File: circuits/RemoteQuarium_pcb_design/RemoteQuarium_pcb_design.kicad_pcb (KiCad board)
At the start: 2 copper layers, 68.6 x 99.1 mm, 20 parts, among them J1 Power_terminal, J10 LCD_pins, J11 Ph_sensor_sockets, J12 ESP_pins, J13 TX_RX, J14 3.3V_GND, J2 ESP left side sockets, J3 ESP right side sockets, J4 Relay_terminal, J5 Relay_in4_socket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

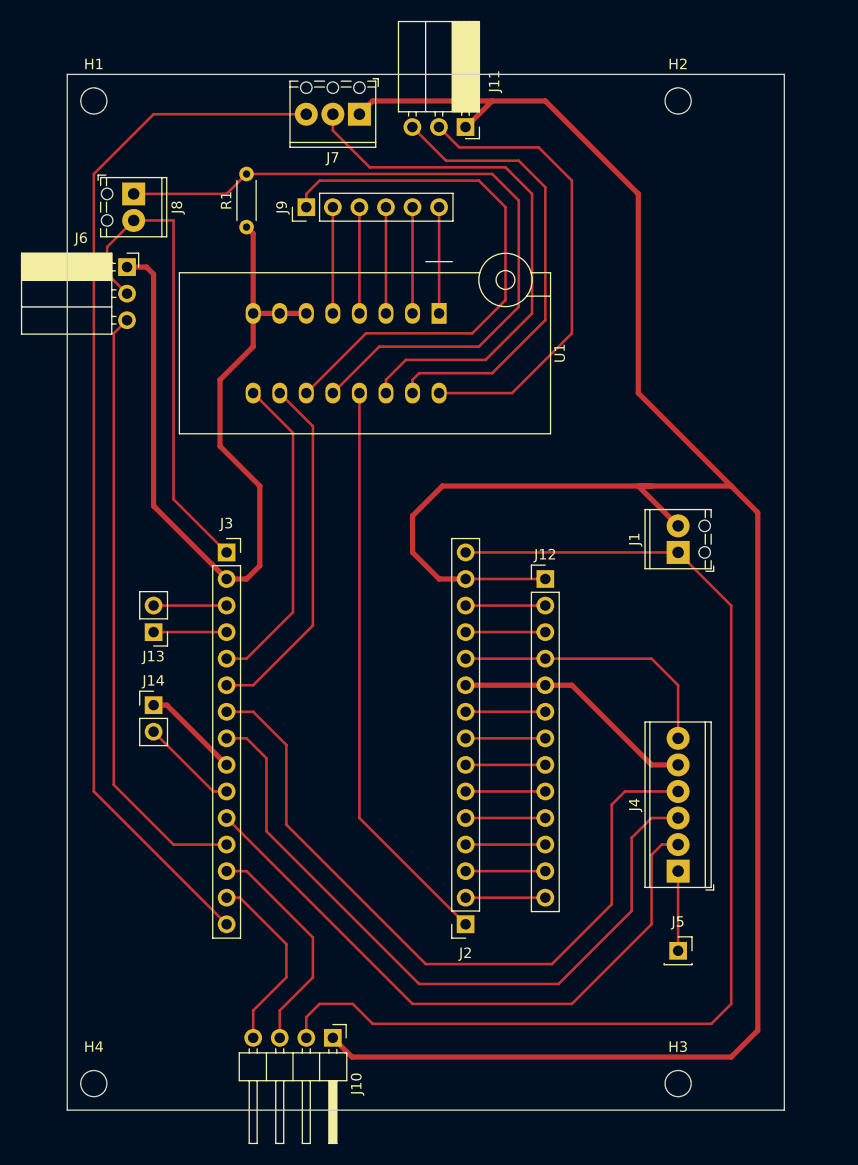
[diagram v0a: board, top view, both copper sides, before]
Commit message: Made PCB plans, it should be double checked but seems ok. Added basic info display to code tested!
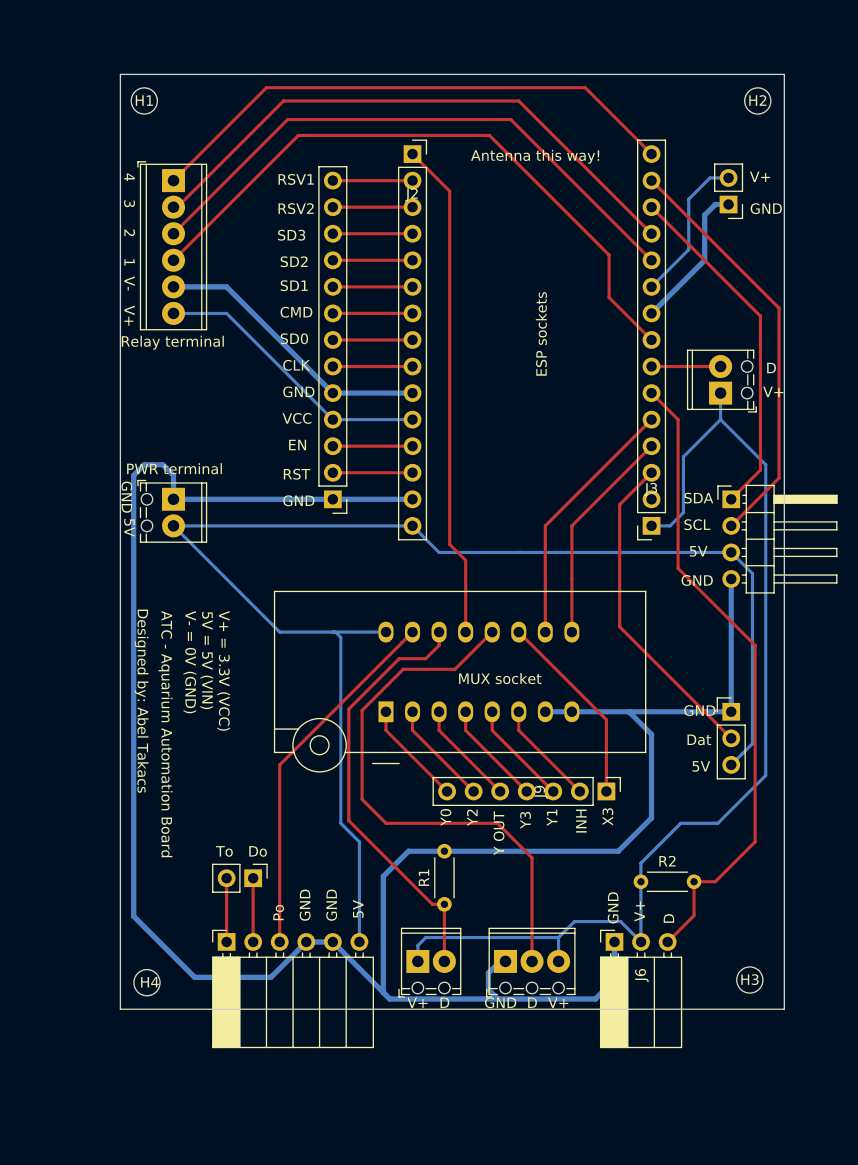
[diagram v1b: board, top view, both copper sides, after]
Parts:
- added J15: Vcc-GND, Connector_PinHeader_2.54mm:PinHeader_1x02_P2.54mm_Vertical, F.Cu at (180.1, 48.0)
- added R2: 4700R, Resistor_THT:R_Axial_DIN0204_L3.6mm_D1.6mm_P5.08mm_Horizontal, F.Cu at (171.7, 112.8)
- J11: value Ph_sensor_sockets -> Feeder_servo_pins; footprint Connector_PinSocket_2.54mm:PinSocket_1x03_P2.54mm_Horizontal -> Connector_PinHeader_2.54mm:PinHeader_1x03_P2.54mm_Vertical
- J13: value TX_RX -> PH_sensor_sockets; footprint Connector_PinHeader_2.54mm:PinHeader_1x02_P2.54mm_Vertical -> Connector_PinSocket_2.54mm:PinSocket_1x06_P2.54mm_Horizontal
- J14: value 3.3V_GND -> Ph_sesnor-pins
- J5: value Relay_in4_socket -> Calibration_btn; footprint Connector_PinSocket_2.54mm:PinSocket_1x01_P2.54mm_Vertical -> TerminalBlock_Phoenix:TerminalBlock_Phoenix_MPT-0,5-2-2.54_1x02_P2.54mm_Horizontal
- J9: footprint Connector_PinHeader_2.54mm:PinHeader_1x06_P2.54mm_Vertical -> Connector_PinHeader_2.54mm:PinHeader_1x07_P2.54mm_Vertical
- moved J7 82.2 mm to (158.8, 120.4), turned to 0 degrees
- moved J4 81.8 mm to (127.0, 45.7), turned to -90 degrees
- moved J6 79.6 mm to (169.2, 118.5), turned to 90 degrees
- moved J8 78.3 mm to (150.4, 120.4), turned to 0 degrees
- moved J2 73.8 mm to (149.9, 43.2), turned to 0 degrees
- moved R1 67.5 mm to (152.9, 114.9)
- moved J10 64.1 mm to (180.3, 76.2), turned to 0 degrees
- moved J9 62.8 mm to (168.4, 104.1), turned to -90 degrees
- moved J11 61.4 mm to (180.3, 96.5), turned to 0 degrees
- moved J5 53.5 mm to (179.3, 66.0), turned to 90 degrees
- moved J1 48.5 mm to (127.0, 76.2), turned to -90 degrees
- moved J3 40.7 mm to (172.7, 78.7), turned to 180 degrees
- moved U1 38.4 mm to (147.3, 96.5), turned to 90 degrees
- moved J13 30.4 mm to (132.1, 118.5), turned to 90 degrees
- moved J12 21.7 mm to (142.2, 76.2), turned to 180 degrees
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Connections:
- J1 pad 1: /VIN -> /GND
- J1 pad 2: /GND -> /VIN
- J10 pad 1: /GND -> /SDA
- J10 pad 2: /VIN -> /SCL
- J10 pad 3: /D2 -> /VIN
- J10 pad 4: /D1 -> /GND
- J11 pad 2: /VCC -> /TX
- J11 pad 3: /Ph_DAT -> /VIN
- J13 pad 1: /RX -> /T0
- J13 pad 2: /TX -> /Do
- J14 pad 1: /GND -> /Do
- J14 pad 2: /VCC -> /T0
- J3 pad 13: /D2 -> /SDA
- J3 pad 14: /D1 -> /SCL
- J4 pad 1: /IN4 -> /D0
- J4 pad 2: /D4 -> /D3
- J4 pad 3: /D5 -> /D4
- J4 pad 4: /D6 -> /D5
- J5 pad 1: /IN4 -> /VCC
- J6 pad 3: /D3 -> /D7
- J7 pad 3: /D0 -> /VCC
- J8 pad 1: /LIGHT_DAT -> /VCC
- J8 pad 2: /VCC -> /LIGHT_DAT
- J9 pad 1: /Y3 -> /X3
- J9 pad 2: /Y2 -> /INH
- J9 pad 4: /Y0 -> /Y3
- J9 pad 5: /Y_out -> /Y
- J9 pad 6: /X3 -> /Y2
- R1 pad 1: /GND -> /LIGHT_DAT
- R1 pad 2: /LIGHT_DAT -> /GND
- U1 pad 1: /X3 -> /Y0
- U1 pad 10: /D7 -> /D8
- U1 pad 11: /Y3 -> /X3
- U1 pad 12: /LIGHT_DAT -> /WATER_DAT
- U1 pad 14: /WATER_DAT -> /LIGHT_DAT
- U1 pad 15: /Ph_DAT -> /P0
- U1 pad 16: /VCC -> /VIN
- U1 pad 2: /Y_out -> /Y2
- U1 pad 3: /Y0 -> /Y
- U1 pad 4: /Y1 -> /Y3
- U1 pad 5: /Y2 -> /Y1
- U1 pad 6: /GND -> /INH
- U1 pad 9: /D8 -> /RX
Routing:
- net /GND: track 329.2 -> 256.1 mm
- net /D6: track 70.1 -> 6.60 mm
- net /D0: track 99.7 -> 52.0 mm
- net /Ph_DAT: track 44.1 -> 0.00 mm
- net /Y3: track 53.5 -> 10.0 mm
- net /SCL: track 0.00 -> 40.0 mm
- net /P0: track 0.00 -> 34.9 mm
- net /SDA: track 0.00 -> 33.4 mm
- net /LIGHT_DAT: track 70.0 -> 40.9 mm
- net /D7: track 34.2 -> 61.3 mm
- net /TX: track 7.62 -> 31.1 mm
- net /D2: track 21.8 -> 0.00 mm
- net /VIN: track 110.3 -> 132.0 mm
- net /D1: track 17.8 -> 0.00 mm
- net /VCC: track 126.8 -> 144.3 mm
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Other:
- board size 68.6 x 99.1 mm -> 63.5 x 89.4 mm
- board text added: "1"
- board text added: "2"
- board text added: "3"
- board text added: "4"
- board text added: "5V"
- board text added: "ATC - Aquarium Automation Board"
- board text added: "Antenna this way!"
- board text added: "CLK"
- board text added: "CMD"
- board text added: "D"
- board text added: "Dat"
- board text added: "Designed by: Abel Takacs"
- board text added: "Do"
- board text added: "EN"
- board text added: "ESP sockets"
- board text added: "GND"
- board text added: "INH"
- board text added: "MUX socket"
- board text added: "PWR terminal"
- board text added: "Po"
- board text added: "RST"
- board text added: "RSV1"
- board text added: "RSV2"
- board text added: "Relay terminal"
- board text added: "SCL"
- board text added: "SD0"
- board text added: "SD1"
- board text added: "SD2"
- board text added: "SD3"
- board text added: "SDA"
- board text added: "To"
- board text added: "V+"
- board text added: "V+ = 3.3V (VCC) 5V = 5V (VIN) V- = 0V (GND)"
- board text added: "V-"
- board text added: "VCC"
- board text added: "X3"
- board text added: "Y OUT"
- board text added: "Y0"
- board text added: "Y1"
- board text added: "Y2"
- board text added: "Y3"

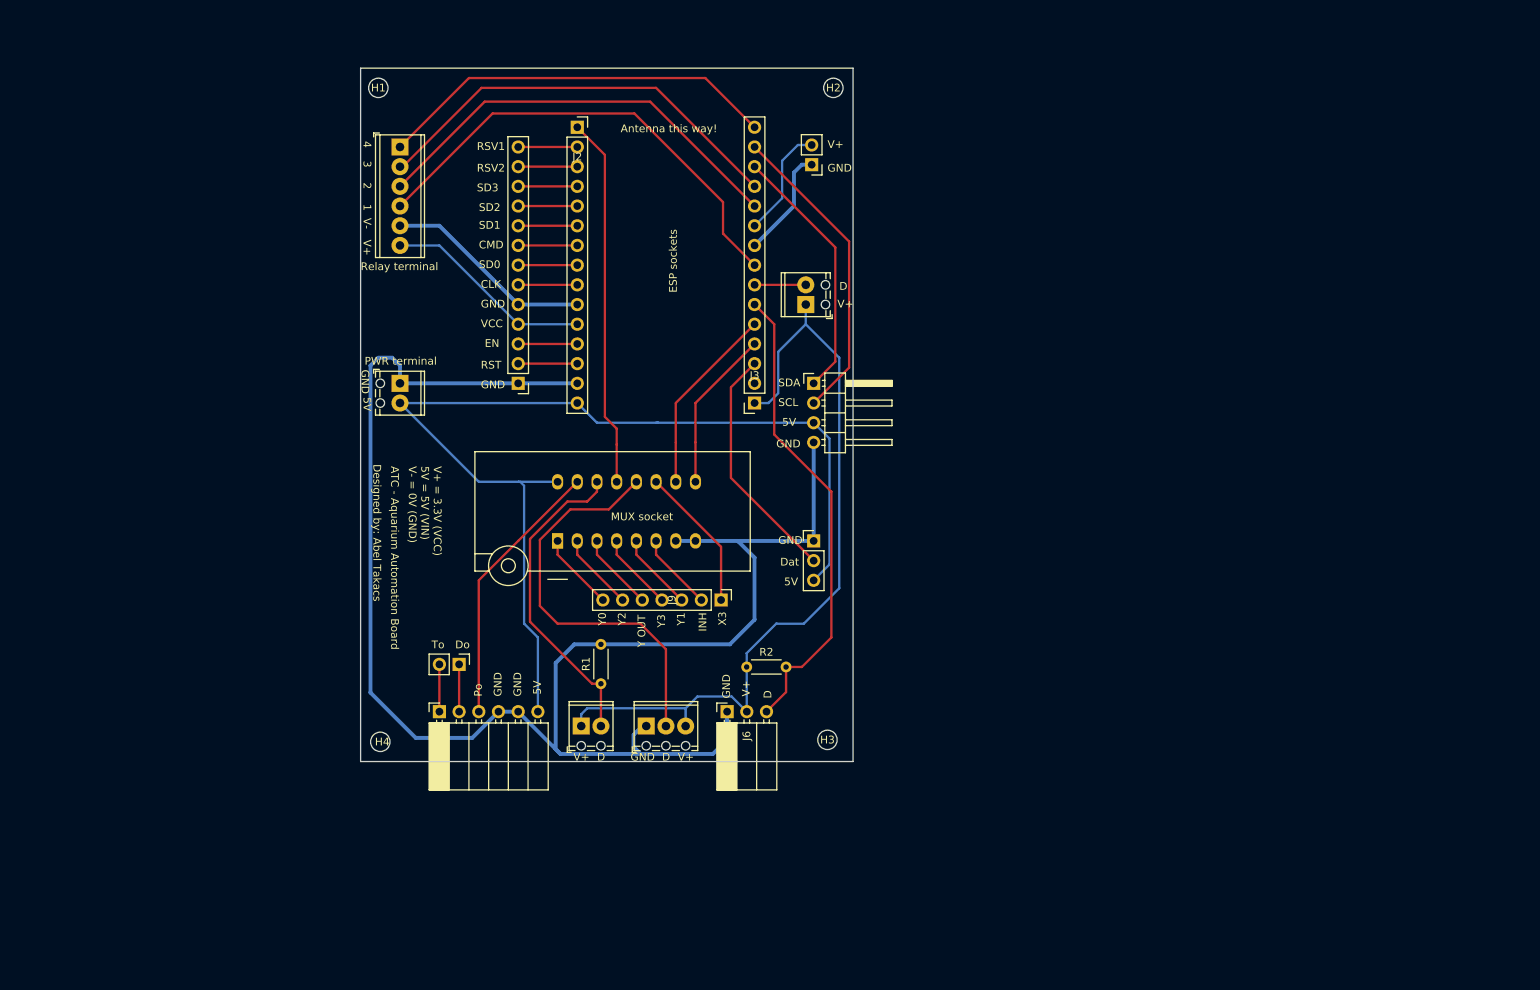
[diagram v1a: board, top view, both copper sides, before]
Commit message: Tested the ESP and added logging. Sensor sample selection is not working, need a solution!
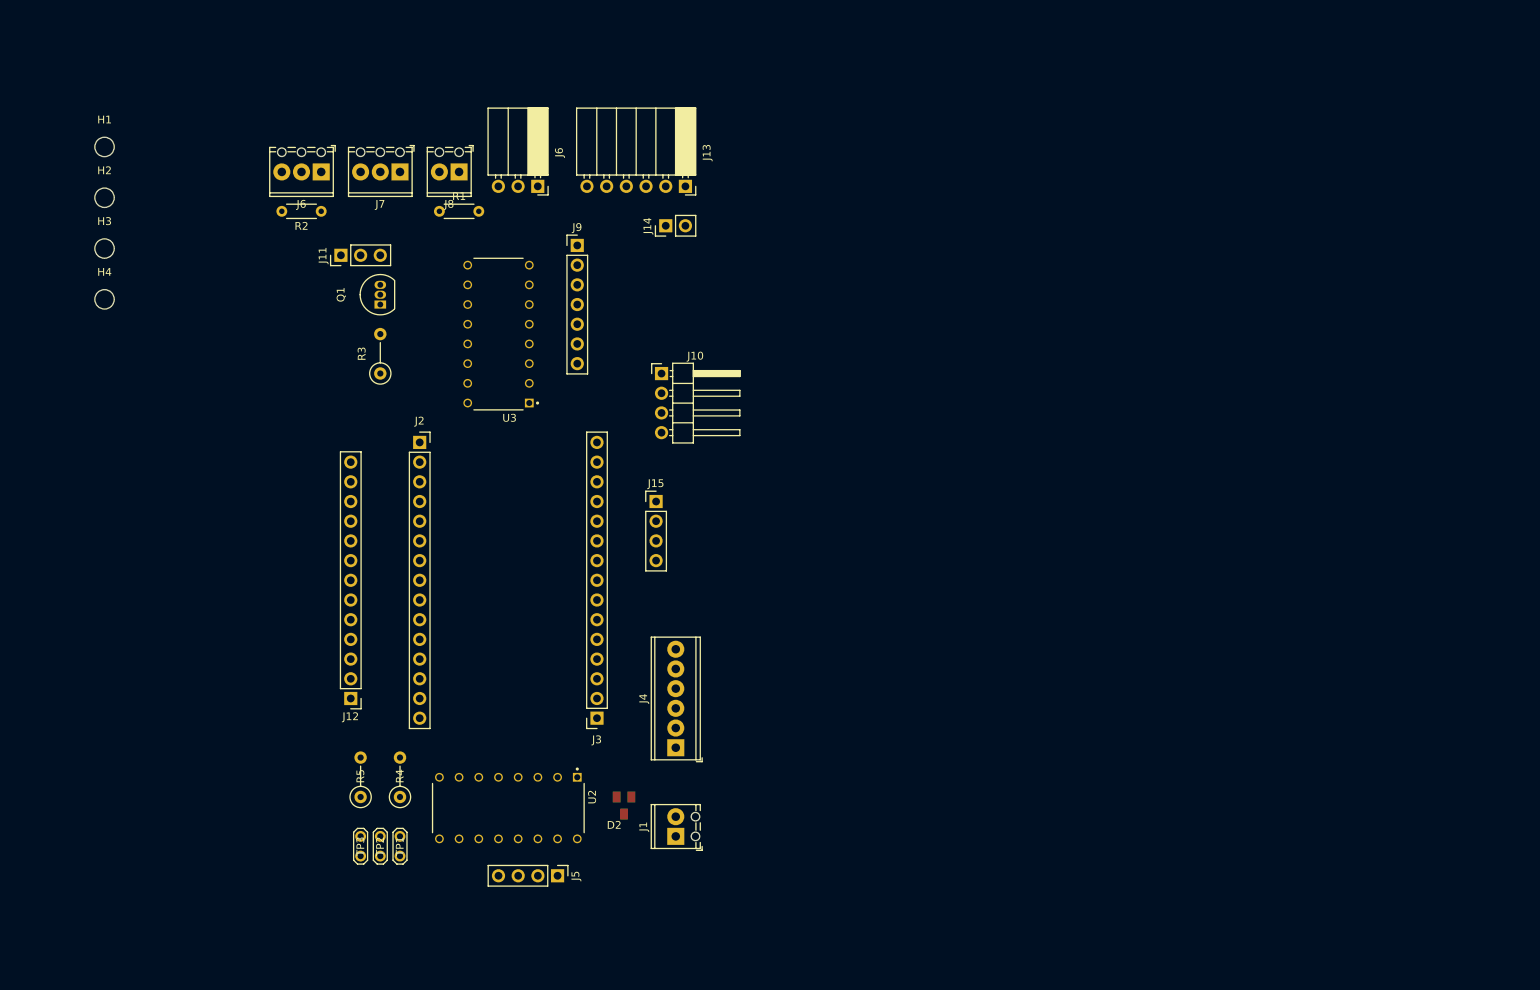
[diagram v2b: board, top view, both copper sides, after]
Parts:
- removed the J6 at (169.2, 118.5)
- removed U1: CD4052BE, Socket:DIP_Socket-16_W4.3_W5.08_W7.62_W10.16_W10.9_3M_216-3340-00-0602J
- added D2: PESD5V0S2BT, PESD5V0S2BT:SOT23, F.Cu at (154.6, 130.6)
- added J6: Temp_sensor_terminal, TerminalBlock_Phoenix:TerminalBlock_Phoenix_MPT-0,5-3-2.54_1x03_P2.54mm_Horizontal, F.Cu at (116.8, 48.9)
- added J6: Temp_sensor_socket, Connector_PinSocket_2.54mm:PinSocket_1x03_P2.54mm_Horizontal, F.Cu at (144.8, 50.8)
- added Q1: BC547, Package_TO_SOT_THT:TO-92_Inline, F.Cu at (124.5, 66.0)
- added R3: 10kR, Resistor_THT:R_Axial_DIN0207_L6.3mm_D2.5mm_P5.08mm_Vertical, F.Cu at (124.5, 74.9)
- added R4: 470R, Resistor_THT:R_Axial_DIN0207_L6.3mm_D2.5mm_P5.08mm_Vertical, F.Cu at (127.0, 129.5)
- added R5: 470R, Resistor_THT:R_Axial_DIN0207_L6.3mm_D2.5mm_P5.08mm_Vertical, F.Cu at (121.9, 129.5)
- added TP1: LED_an_G, TestPoint:TestPoint_2Pads_Pitch2.54mm_Drill0.8mm, F.Cu at (127.0, 134.6)
- added TP2: LED_common_cat, TestPoint:TestPoint_2Pads_Pitch2.54mm_Drill0.8mm, F.Cu at (124.5, 134.6)
- added TP3: LED_an_R, TestPoint:TestPoint_2Pads_Pitch2.54mm_Drill0.8mm, F.Cu at (121.9, 134.6)
- added U2: 74HC595, CD4052BE:DIP794W45P254L1969H508Q16, F.Cu at (141.0, 131.0)
- added U3: CD4052B, CD4052BE:DIP794W45P254L1969H508Q16, F.Cu at (139.7, 69.8)
- J15: value Vcc-GND -> Power & D3-D4; footprint Connector_PinHeader_2.54mm:PinHeader_1x02_P2.54mm_Vertical -> Connector_PinHeader_2.54mm:PinHeader_1x04_P2.54mm_Vertical
- J5: value Calibration_btn -> SREG_pins; footprint TerminalBlock_Phoenix:TerminalBlock_Phoenix_MPT-0,5-2-2.54_1x02_P2.54mm_Horizontal -> Connector_PinHeader_2.54mm:PinHeader_1x04_P2.54mm_Vertical
- R1: value 10000 -> 10kR
- moved H3 112.7 mm to (88.9, 58.8)
- moved H2 95.0 mm to (88.9, 52.3)
- moved J4 85.2 mm to (162.6, 123.2), turned to 90 degrees
- moved R2 80.4 mm to (116.8, 54.0), turned to 180 degrees
- moved J5 80.3 mm to (147.3, 139.7), turned to -90 degrees
- moved J7 78.2 mm to (127.0, 48.9), turned to 180 degrees
- moved J13 74.8 mm to (163.8, 50.8), turned to -90 degrees
- moved J8 73.2 mm to (134.6, 48.9), turned to 180 degrees
- moved J11 71.2 mm to (119.4, 59.7), turned to 90 degrees
- moved J1 68.4 mm to (162.6, 134.6), turned to 90 degrees
- moved H4 67.2 mm to (88.9, 65.4)
- moved R1 64.4 mm to (132.1, 54.0), turned to 0 degrees
- moved J14 62.5 mm to (161.3, 55.9), turned to 90 degrees
- moved J9 49.3 mm to (149.9, 58.4), turned to 0 degrees
- moved J15 47.8 mm to (160.0, 91.4), turned to 0 degrees
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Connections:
- J15 pad 1: /GND -> /D3
- J15 pad 2: /VCC -> /D4
- J4 pad 1: /D0 -> /S0
- J4 pad 2: /D3 -> /S1
- J4 pad 3: /D4 -> /S2
- J4 pad 4: /D5 -> /S3
- J5 pad 1: /VCC -> /QA
- J5 pad 2: /D6 -> /QG
- J9 pad 1: /X3 -> /Y
- J9 pad 3: /Y1 -> /X3
- J9 pad 5: /Y -> /Y2
- J9 pad 6: /Y2 -> /Y1
- R1 pad 2: /GND -> /LIGHT_DAT
- R2 pad 2: /D7 -> /RX
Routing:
- net /GND: track 256.1 -> 0.00 mm
- net /VCC: track 144.3 -> 0.00 mm
- net /VIN: track 132.0 -> 0.00 mm
- net /D7: track 61.3 -> 0.00 mm
- net /D5: track 61.1 -> 0.00 mm
- net /D4: track 55.8 -> 0.00 mm
- net /D3: track 55.2 -> 0.00 mm
- net /WATER_DAT: track 52.5 -> 0.00 mm
- net /D0: track 52.0 -> 0.00 mm
- net /A0: track 47.8 -> 0.00 mm
- net /LIGHT_DAT: track 40.9 -> 0.00 mm
- net /SCL: track 40.0 -> 0.00 mm
- net /P0: track 34.9 -> 0.00 mm
- net /SDA: track 33.4 -> 0.00 mm
- net /TX: track 31.1 -> 0.00 mm
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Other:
- board outline removed
- board text removed: "1"
- board text removed: "2"
- board text removed: "3"
- board text removed: "4"
- board text removed: "5V"
- board text removed: "ATC - Aquarium Automation Board"
- board text removed: "Antenna this way!"
- board text removed: "CLK"
- board text removed: "CMD"
- board text removed: "D"
- board text removed: "Dat"
- board text removed: "Designed by: Abel Takacs"
- board text removed: "Do"
- board text removed: "EN"
- board text removed: "ESP sockets"
- board text removed: "GND"
- board text removed: "INH"
- board text removed: "MUX socket"
- board text removed: "PWR terminal"
- board text removed: "Po"
- board text removed: "RST"
- board text removed: "RSV1"
- board text removed: "RSV2"
- board text removed: "Relay terminal"
- board text removed: "SCL"
- board text removed: "SD0"
- board text removed: "SD1"
- board text removed: "SD2"
- board text removed: "SD3"
- board text removed: "SDA"
- board text removed: "To"
- board text removed: "V+"
- board text removed: "V+ = 3.3V (VCC) 5V = 5V (VIN) V- = 0V (GND)"
- board text removed: "V-"
- board text removed: "VCC"
- board text removed: "X3"
- board text removed: "Y OUT"
- board text removed: "Y0"
- board text removed: "Y1"
- board text removed: "Y2"
- board text removed: "Y3"
